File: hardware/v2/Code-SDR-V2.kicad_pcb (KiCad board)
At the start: 4 copper layers, 160 x 100 mm, 344 parts, among them J1 5V_INPUT_ONLY, J10 USB_B_Micro, J11 Cortex_SWD_10pin, J30 JK0654219NL, J50 RF_LOW_0.1_2.5GHz, J60 RF_HIGH_2.3_4.2GHz, J61 RF_HIGH_4.2_6.8GHz, J62 RF_HIGH_6.8_9.2GHz, J63 RF_HIGH_8.0_10GHz, SW1 BOOTSEL, SW2 RESET, T50 2450BL15B0200001E, T60 TC1-1-13M+, T70 2450BL15B0100001E, U1 TLV62569DBVR, U10 RP2040, U11 W25Q16JVSSIQ, U12 USBLC6-2SC6, U2 TLV62569DBVR, U20 LIF-MD6000-6JMG80I, U21 AD9215BCPZ-105, U3 TLV75525PDBVR, U30 KSZ9031RNXCA, U4 TLV76733DRVR, U40 LMX2592RHAT, U41 ADF4360-1BCPZ, U42 CDCLVC1104PWR, U50 GRF4001, U51 ADL5801ACPZ-R7, U60 GRF4001, U61 GRF2101, U62 GRF2101, U63 LTC5548IUDB, U64 QPC6144TR13, U66 GRF2101, U67 GRF2101, U70 BGS12WN6E6327, U71 GRF2013, U72 PE4312C-Z, U73 LT5560EDD, U74 AD8351ARMZ, U75 GRF2013, Y10 ABM8-272-T3_12MHz, Y30 ECS-250-20-33-TR_25MHz, Y40 SiT8209AC-23-33E-100.000000X

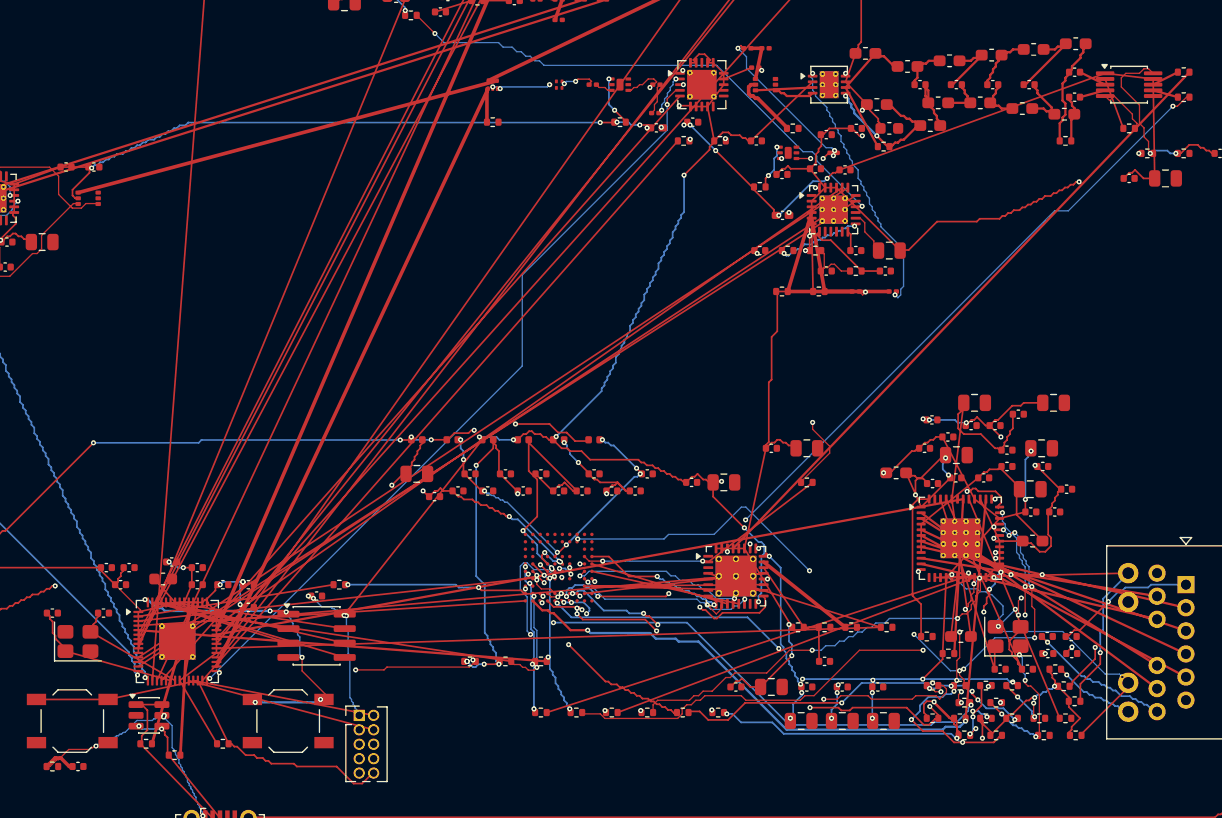
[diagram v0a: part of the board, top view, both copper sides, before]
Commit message: chore(hardware): re-route RGMII/MDI/PHY congestion cluster (40 nets)
Targeted the Ethernet PHY/magnetics area directly this time (previously
skipped as 'expected adjacency' but investigation showed genuine
clearance conflicts between unrelated nets there, not just the
documented resistor-bridge pattern). Verified 0 nets with zero copper
before zone refill.
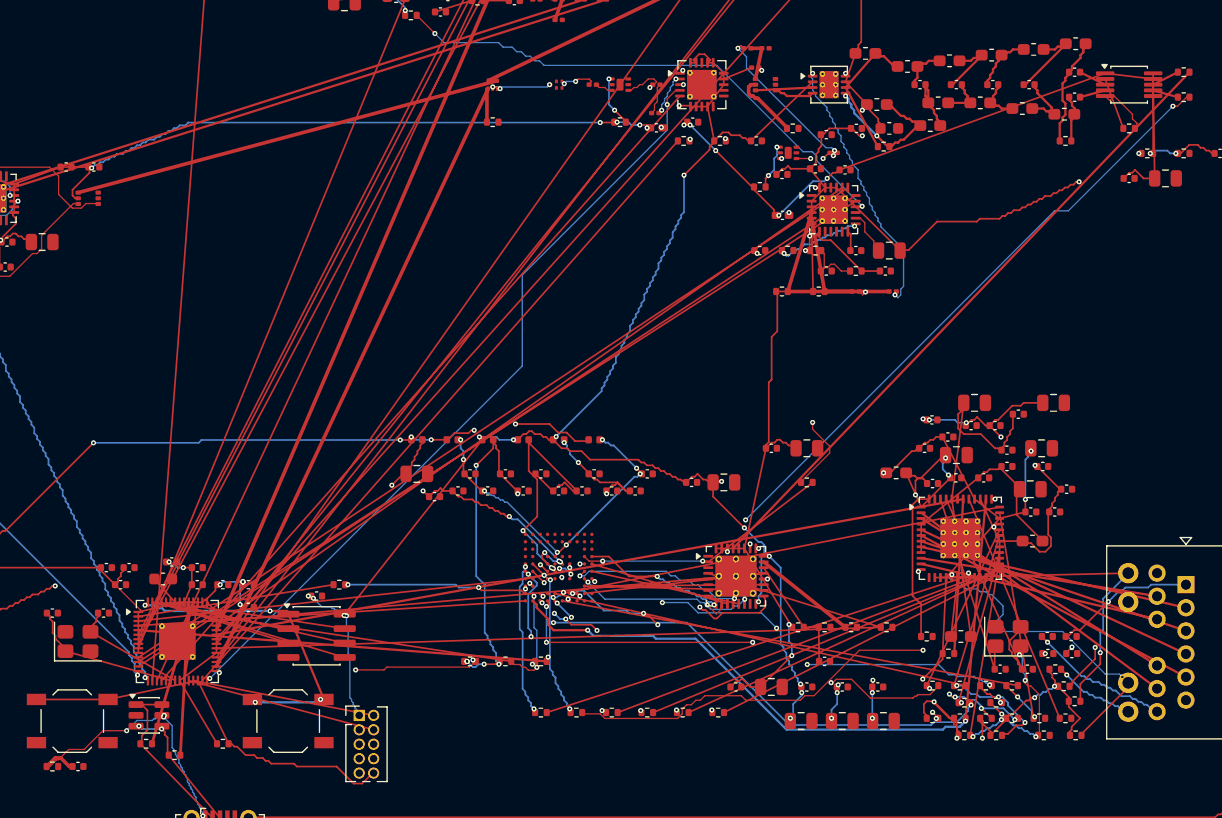
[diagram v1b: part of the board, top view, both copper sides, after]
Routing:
- net RGMII_TXC: track 47.4 -> 26.4 mm, vias 5 -> 0
- net RGMII_RXD0_FPGA: track 56.1 -> 39.6 mm
- net RGMII_RXD1_FPGA: track 50.2 -> 37.0 mm, vias 6 -> 0
- net RGMII_RXD0: track 32.8 -> 24.4 mm, vias 11 -> 4
- net MDC: track 46.2 -> 39.2 mm, vias 4 -> 0
- net RGMII_RXD1: track 30.4 -> 24.1 mm, vias 9 -> 2
- net RGMII_TX_EN: track 35.6 -> 30.1 mm, vias 5 -> 0
- net RGMII_RXD2: track 22.0 -> 17.5 mm, vias 7 -> 2
- net RGMII_TXD3: track 35.4 -> 31.1 mm, vias 2 -> 0
- net ADC_VCM: track 18.1 -> 13.9 mm
- net RGMII_RXC_FPGA: track 44.0 -> 40.8 mm, vias 4 -> 0
- net RGMII_RX_DV_FPGA: track 44.9 -> 46.7 mm
- net QSPI_SS_N: track 29.6 -> 28.0 mm, vias 6 -> 4
- net RGMII_TXD2_FPGA: track 15.4 -> 16.5 mm, vias 2 -> 3
- net RGMII_RXC: track 23.4 -> 22.4 mm, vias 6 -> 2
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
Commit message: chore(hardware): seventh DRC cleanup sweep (40 nets)
Continued targeting top offenders including remaining RGMII/PHY cluster
members and power nets. Verified 0 nets with zero copper before zone
refill.
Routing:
- net RGMII_TXD1: track 42.3 -> 36.0 mm, vias 2 -> 0
- net RGMII_TXC_FPGA: track 19.6 -> 16.4 mm, vias 4 -> 0
- net RGMII_RX_DV: track 28.0 -> 25.0 mm, vias 5 -> 2
- net RGMII_RXC_FPGA: track 40.8 -> 43.4 mm, vias 0 -> 4
- net RGMII_TXD1_FPGA: track 14.3 -> 16.5 mm, vias 2 -> 3
- net ADC_D5: track 15.9 -> 14.2 mm, vias 2 -> 0
- net FPGA_VCCIO1_3V3: track 26.2 -> 25.1 mm
- net PHY_XO: track 21.0 -> 20.1 mm
- net RGMII_RXD3: track 24.2 -> 23.6 mm, vias 3 -> 2
- net FPGA_VCCIO2_3V3: track 20.8 -> 20.3 mm, vias 6 -> 4
- net RGMII_RXD0_FPGA: track 39.6 -> 39.9 mm, vias 5 -> 3
- net PHY_AVDDL_1V2: track 19.5 -> 19.3 mm, vias 0 -> 2
- net RGMII_TX_EN_FPGA: track 16.8 -> 16.6 mm, vias 5 -> 2
- net RGMII_RXD0: vias 4 -> 2
- net MAG_CT3: vias 1 -> 2

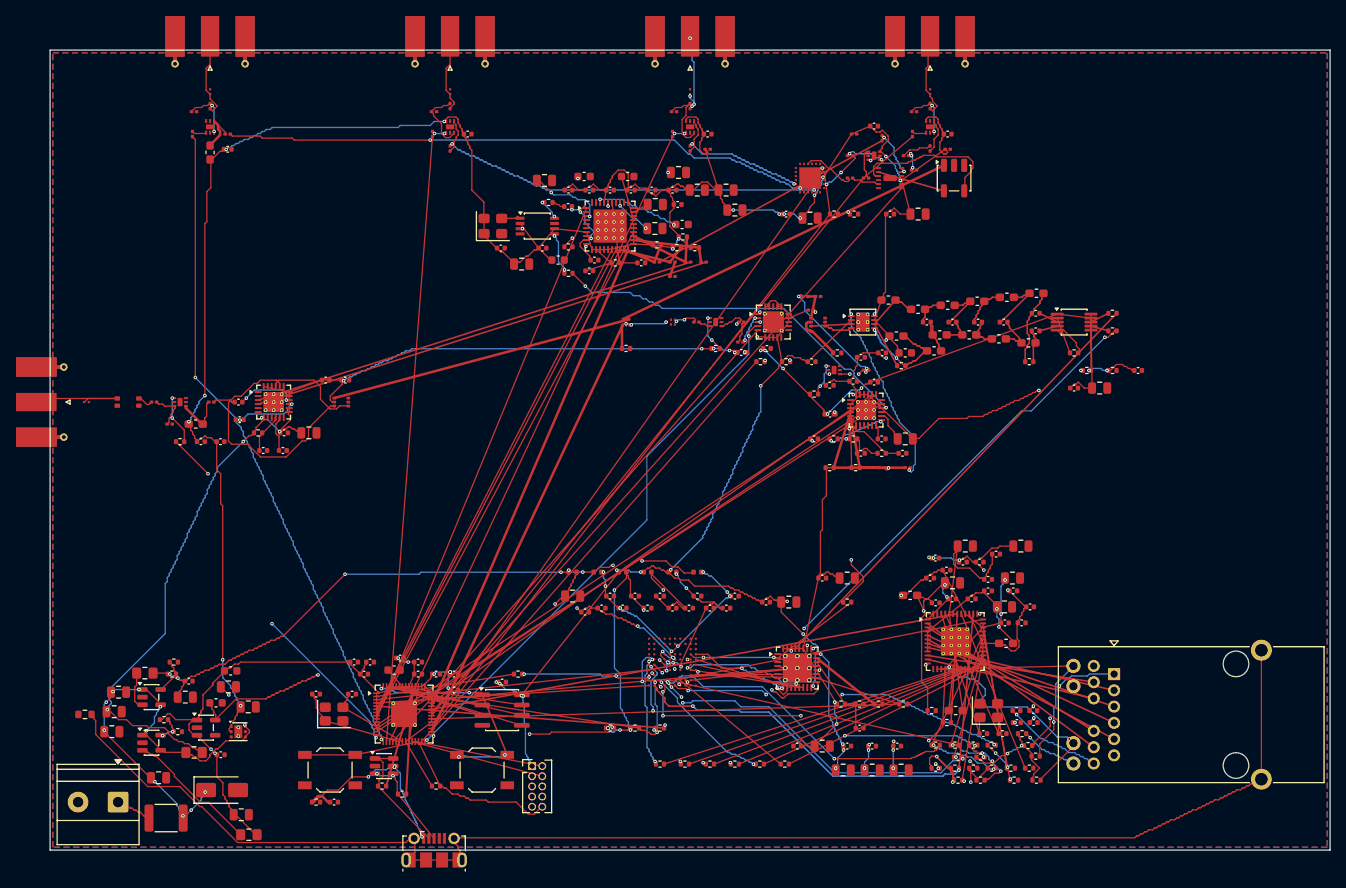
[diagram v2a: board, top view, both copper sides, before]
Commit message: chore(hardware): eighth DRC cleanup sweep (40 nets)
Re-attempted power nets (converged to same local optimum) plus 36 more
offending nets from latest DRC report. Verified 0 nets with zero copper
before zone refill.
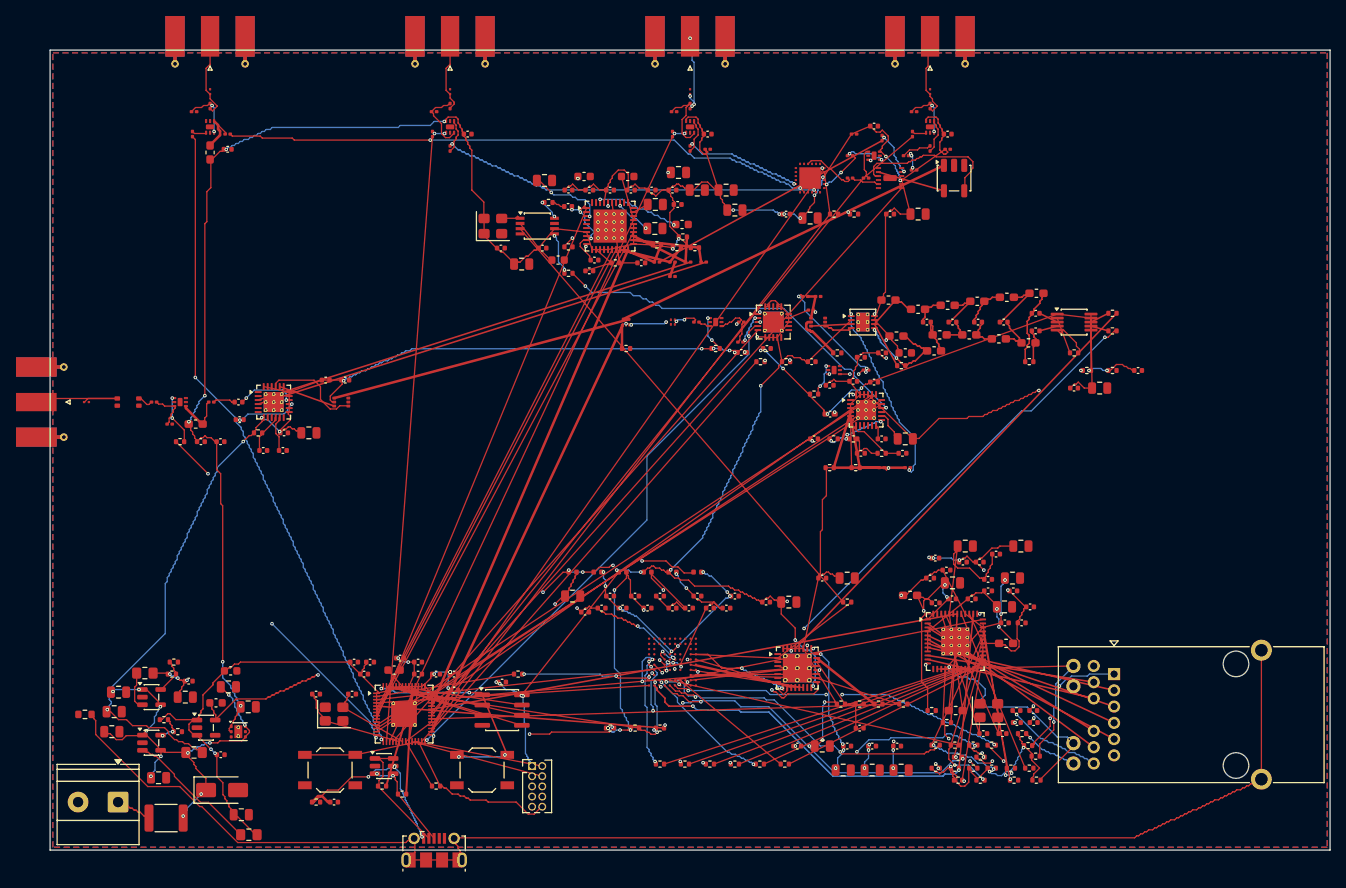
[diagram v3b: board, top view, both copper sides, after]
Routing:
- net IF_LOW_P: track 30.3 -> 7.24 mm
- net VIN_FUSED: track 60.5 -> 54.6 mm
- net REF_100M_ADC: track 65.7 -> 61.7 mm, vias 2 -> 0
- net +3V3_DIG: track 336.0 -> 333.2 mm, vias 31 -> 29
- net RGMII_RXD1: track 24.1 -> 21.3 mm
- net RGMII_RXC: track 22.4 -> 24.8 mm, vias 2 -> 3
- net ADC_D3: track 15.7 -> 13.4 mm, vias 2 -> 0
- net RGMII_RX_DV_FPGA: track 46.7 -> 44.9 mm, vias 3 -> 2
- net RGMII_RXD0_FPGA: track 39.9 -> 39.5 mm, vias 3 -> 2
- net RGMII_RXD3_FPGA: track 44.7 -> 44.4 mm, vias 5 -> 3
- net ADC_CLK: track 22.5 -> 22.4 mm, vias 2 -> 0
- net +3V3_ANA: track 407.3 -> 407.4 mm, vias 22 -> 24
